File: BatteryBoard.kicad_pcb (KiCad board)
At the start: 4 copper layers, 90.2 x 95.9 mm, 134 parts, among them J1 Keystone-1048, J10 200528-0100, J5 Keystone-1042, J6 Keystone-1042, J7 1824543, J8 Conn_01x06, J9 Keystone-1048, Q1 NX3008NBKS, Q2 MBT2222ADW1T1, Q3 NX3008NBKS, Q4 MBT2222ADW1T1, Q5 NX3008NBKS, Q6 MBT2222ADW1T1, Q7 NX3008NBKS, Q8 MBT2222ADW1T1, U1 S-8209AAA-T8T1U, U10 BTS5090-1EJA, U11 BTS5090-1EJA, U12 PCA9536D, U2 S-8209AAA-T8T1U, U3 MAX17205G+, U4 SIRA99DP-T1-GE3, U5 SIRA99DP-T1-GE3, U6 SIRA99DP-T1-GE3, U7 SIRA99DP-T1-GE3, U8 LTC4412xS6, U9 LTC4412xS6

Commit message: v2.1 (v3?) Partial Updates
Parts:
- removed F10, F12: 10A, Fuse:Fuse_1206_3216Metric
- removed the J7 at (171.0, 99.9)
- removed J8: Conn_01x06, Connector_PinHeader_2.54mm:PinHeader_1x06_P2.54mm_Vertical
- removed U10, U11: BTS5090-1EJA, Package_SO:Infineon_PG-DSO-8-43
- removed U12: PCA9536D, Package_SO:SOIC-8_3.9x4.9mm_P1.27mm
- removed U8, U9: LTC4412xS6, Package_TO_SOT_SMD:TSOT-23-6
- added D8: MMBD452LT1G, Package_TO_SOT_SMD:SOT-23-3, B.Cu at (107.6, 93.9)
- added D9: MMBD452LT1G, Package_TO_SOT_SMD:SOT-23-3, B.Cu at (107.6, 100.7)
- added F5: 10A, Fuse:Fuse_1206_3216Metric, B.Cu at (182.1, 76.7)
- added F8: 6A, Fuse:Fuse_1206_3216Metric, B.Cu at (164.1, 110.2)
- added J5: Fuel Gauge Programming Header, Connector_PinHeader_2.54mm:PinHeader_1x05_P2.54mm_Vertical_SMD_Pin1Left, B.Cu at (160.1, 86.1)
- added Q11: SIRA99DP-T1-GE3, Package_SO:PowerPAK_SO-8_Single, B.Cu at (172.5, 108.9)
- added Q12: SIRA99DP-T1-GE3, Package_SO:PowerPAK_SO-8_Single, B.Cu at (172.5, 101.6)
- added Q13: SIRA99DP-T1-GE3, Package_SO:PowerPAK_SO-8_Single, B.Cu at (160.2, 108.9)
- added Q14: SIRA99DP-T1-GE3, Package_SO:PowerPAK_SO-8_Single, B.Cu at (160.2, 101.7)
- added Q15: NX3008NBKS, Package_TO_SOT_SMD:SOT-363_SC-70-6, B.Cu at (141.4, 80.8)
- added Q16: MBT2222ADW1T1, Package_TO_SOT_SMD:SOT-363_SC-70-6, B.Cu at (145.4, 80.8)
- added Q17: NX3008NBKS, Package_TO_SOT_SMD:SOT-363_SC-70-6, B.Cu at (145.4, 85.6)
- added Q18: MBT2222ADW1T1, Package_TO_SOT_SMD:SOT-363_SC-70-6, B.Cu at (141.4, 85.6)
- added Q19: NX3008NBKS, Package_TO_SOT_SMD:SOT-363_SC-70-6, B.Cu at (125.8, 80.8)
- added Q20: MBT2222ADW1T1, Package_TO_SOT_SMD:SOT-363_SC-70-6, B.Cu at (130.2, 80.8)
- added Q21: NX3008NBKS, Package_TO_SOT_SMD:SOT-363_SC-70-6, B.Cu at (130.2, 85.6)
- added Q22: MBT2222ADW1T1, Package_TO_SOT_SMD:SOT-363_SC-70-6, B.Cu at (125.8, 85.6)
- added Q23: IRLML2803, Package_TO_SOT_SMD:SOT-23, B.Cu at (135.3, 110.6)
- added Q9: Si1442DH, Package_TO_SOT_SMD:SOT-363_SC-70-6, B.Cu at (99.4, 61.2)
- added R62: 10k, Resistor_SMD:R_0603_1608Metric, B.Cu at (141.5, 83.2)
- added R63: 680R, Resistor_SMD:R_0603_1608Metric, B.Cu at (147.4, 80.8)
- added R64: 100k, Resistor_SMD:R_0603_1608Metric, B.Cu at (138.4, 83.2)
- added R65: 200k, Resistor_SMD:R_0603_1608Metric, B.Cu at (138.4, 81.7)
- added R66: 10k, Resistor_SMD:R_0603_1608Metric, B.Cu at (137.8, 85.6)
- added R67: 10k, Resistor_SMD:R_0603_1608Metric, B.Cu at (145.3, 83.2)
- added R68: 680R, Resistor_SMD:R_0603_1608Metric, B.Cu at (139.3, 85.6)
- added R69: 100k, Resistor_SMD:R_0603_1608Metric, B.Cu at (148.3, 83.2)
- added R70: 200k, Resistor_SMD:R_0603_1608Metric, B.Cu at (148.3, 84.7)
- added R71: DNI (0R), Resistor_SMD:R_0603_1608Metric, B.Cu at (143.4, 80.8)
- added R72: DNI (0R), Resistor_SMD:R_0603_1608Metric, B.Cu at (143.4, 85.6)
- added R73: 10k, Resistor_SMD:R_0603_1608Metric, B.Cu at (125.4, 91.4)
- added R74: 10k, Resistor_SMD:R_0603_1608Metric, B.Cu at (125.4, 93.0)
- added R75: 10k, Resistor_SMD:R_0603_1608Metric, B.Cu at (125.4, 94.5)
- added R76: 10k, Resistor_SMD:R_0603_1608Metric, B.Cu at (125.4, 96.0)
- added R77: 10k, Resistor_SMD:R_0603_1608Metric, B.Cu at (125.4, 97.5)
- added R78: 10k, Resistor_SMD:R_0603_1608Metric, B.Cu at (125.4, 99.1)
- added R79: 10k, Resistor_SMD:R_0603_1608Metric, B.Cu at (117.3, 92.9)
- added R80: 10k, Resistor_SMD:R_0603_1608Metric, B.Cu at (133.8, 80.8)
- added R81: 10k, Resistor_SMD:R_0603_1608Metric, B.Cu at (126.0, 83.2)
- added R82: 680R, Resistor_SMD:R_0603_1608Metric, B.Cu at (132.3, 80.8)
- added R83: 100k, Resistor_SMD:R_0603_1608Metric, B.Cu at (122.9, 83.2)
- added R84: 200k, Resistor_SMD:R_0603_1608Metric, B.Cu at (122.9, 81.7)
- added R85: 10k, Resistor_SMD:R_0603_1608Metric, B.Cu at (122.2, 85.6)
- added R86: 10k, Resistor_SMD:R_0603_1608Metric, B.Cu at (130.0, 83.2)
- added R87: 680R, Resistor_SMD:R_0603_1608Metric, B.Cu at (123.7, 85.6)
- added R88: 100k, Resistor_SMD:R_0603_1608Metric, B.Cu at (133.1, 83.2)
- added R89: 200k, Resistor_SMD:R_0603_1608Metric, B.Cu at (133.1, 84.7)
- added R90: DNI (0R), Resistor_SMD:R_0603_1608Metric, B.Cu at (128.0, 80.8)
- added R91: DNI (0R), Resistor_SMD:R_0603_1608Metric, B.Cu at (128.0, 85.6)
- C10: value 0.1uF -> 1nF
- C12, C13: value 10nF -> 0.47uF
- C17, C18: value 10uF -> 10nF; footprint Capacitor_SMD:C_0805_2012Metric -> Capacitor_SMD:C_0603_1608Metric
- C5, C6: value 1nF -> 1uF
- C8: value 0.47uF -> 0.1uF
- C9: value 0.47uF -> 1nF
- D1: value 4.7V -> 10V Vrm; footprint Diode_SMD:D_SMA -> Diode_SMD:D_SOD-123F
- D2: value 10V -> 10V Vrm; footprint Diode_SMD:D_SMA -> Diode_SMD:D_SOD-123F
- D3, D4: value MMBD452LT1G -> GREEN; footprint Package_TO_SOT_SMD:SOT-23-3 -> LED_SMD:LED_0603_1608Metric
- D5: value MMBD452LT1G -> 10V; footprint Package_TO_SOT_SMD:SOT-23-3 -> Diode_SMD:D_SMA
- D6: value 10V Vrm -> 4.7V; footprint Diode_SMD:D_SOD-123F -> Diode_SMD:D_SMA
- D7: value 10V Vrm -> MMBD452LT1G; footprint Diode_SMD:D_SOD-123F -> Package_TO_SOT_SMD:SOT-23-3
- F1: value 1A -> 10A; footprint Fuse:Fuse_0805_2012Metric -> Fuse:Fuse_1206_3216Metric; moved to F.Cu
- F2: value 6A -> 10A; footprint Fuse:Fuse_0805_2012Metric -> Fuse:Fuse_1206_3216Metric; moved to F.Cu
- F3: value 6A -> 10A; footprint Fuse:Fuse_0805_2012Metric -> Fuse:Fuse_1206_3216Metric
- F7: value 10A -> 6A; moved to B.Cu
- F9: value 10A -> 1A; footprint Fuse:Fuse_1206_3216Metric -> Fuse:Fuse_0805_2012Metric; moved to B.Cu
- Q1: value NX3008NBKS -> IRLML2803; footprint Package_TO_SOT_SMD:SOT-363_SC-70-6 -> Package_TO_SOT_SMD:SOT-23
- Q2, Q4: value MBT2222ADW1T1 -> SIRA99DP-T1-GE3; footprint Package_TO_SOT_SMD:SOT-363_SC-70-6 -> Package_SO:PowerPAK_SO-8_Single
- Q3, Q5, Q7: value NX3008NBKS -> Si1442DH; moved to F.Cu
- Q6: value MBT2222ADW1T1 -> Si1442DH; moved to F.Cu
- Q8: value MBT2222ADW1T1 -> Si1442DH
- R10: value 30k -> 100k
- R11: value 30k -> 10k
- R12: value 100K -> 0.05R; footprint Resistor_SMD:R_0603_1608Metric -> Resistor_SMD:R_1206_3216Metric
- R13: value 100K -> 0R
- R14: value 680R -> 10k
- R15: value 100K -> 30k
- R16, R17: value 10K -> 10k
- R18, R39: value 200K -> 10k
- R19: value DNI (0R) -> 2.7k
- R20, R33, R34: value DNI (0R) -> 10R; footprint Resistor_SMD:R_0603_1608Metric -> Resistor_SMD:R_2010_5025Metric; moved to F.Cu
- R21: value 680R -> 10R; footprint Resistor_SMD:R_0603_1608Metric -> Resistor_SMD:R_2010_5025Metric; moved to F.Cu
- R22, R36: value 100K -> 10R; footprint Resistor_SMD:R_0603_1608Metric -> Resistor_SMD:R_2010_5025Metric; moved to F.Cu
- R23, R31: value 10K -> 10k; moved to F.Cu
- R24, R37, R38: value 10K -> 10R; footprint Resistor_SMD:R_0603_1608Metric -> Resistor_SMD:R_2010_5025Metric; moved to F.Cu
- R25, R32: value 200K -> 10R; footprint Resistor_SMD:R_0603_1608Metric -> Resistor_SMD:R_2010_5025Metric; moved to F.Cu
- R26: value 1k -> 10R; footprint Resistor_SMD:R_0603_1608Metric -> Resistor_SMD:R_2010_5025Metric; moved to F.Cu
- R27: value 1k -> 10k
- R28: value 680R -> 10R; footprint Resistor_SMD:R_0603_1608Metric -> Resistor_SMD:R_2010_5025Metric
- R29: value 100K -> 10R; footprint Resistor_SMD:R_0603_1608Metric -> Resistor_SMD:R_2010_5025Metric
- R3: value 10R -> 470R
- R30: value 10K -> 10R; footprint Resistor_SMD:R_0603_1608Metric -> Resistor_SMD:R_2010_5025Metric
- R35: value 680R -> 10k; moved to F.Cu
- R4, R5: value 470R -> 1k
- R40, R41: value 160R -> 10R; moved to B.Cu
- R42: value 160R -> 10R
- R43: value 160R -> 10k; footprint Resistor_SMD:R_2010_5025Metric -> Resistor_SMD:R_0603_1608Metric; moved to F.Cu
- R44: value 160R -> 470k; footprint Resistor_SMD:R_2010_5025Metric -> Resistor_SMD:R_0603_1608Metric; moved to B.Cu
- R45: value 160R -> 100k; footprint Resistor_SMD:R_2010_5025Metric -> Resistor_SMD:R_0603_1608Metric; moved to B.Cu
- R47: value 100k -> 470k; footprint Capacitor_SMD:C_0603_1608Metric -> Resistor_SMD:R_0603_1608Metric
- R48: value 100k -> 10R
- R49: value 100k -> 100R; footprint Capacitor_SMD:C_0603_1608Metric -> Resistor_SMD:R_0603_1608Metric
- R50: value 160R -> 10m; footprint Resistor_SMD:R_2010_5025Metric -> Resistor_SMD:R_2512_6332Metric; moved to B.Cu
- R51: value 160R -> 1k; footprint Resistor_SMD:R_2010_5025Metric -> Resistor_SMD:R_0603_1608Metric; moved to B.Cu
- R52, R53: value 160R -> 30k; footprint Resistor_SMD:R_2010_5025Metric -> Resistor_SMD:R_0603_1608Metric
- R54: value 160R -> 51.1k; footprint Resistor_SMD:R_2010_5025Metric -> Resistor_SMD:R_0603_1608Metric; moved to B.Cu
- R55, R56, R57: value 160R -> 150R; footprint Resistor_SMD:R_2010_5025Metric -> Resistor_SMD:R_0603_1608Metric; moved to B.Cu
- R58: value 160R -> 10k; footprint Resistor_SMD:R_2010_5025Metric -> Resistor_SMD:R_0603_1608Metric
- R59: value 160R -> 0R; footprint Resistor_SMD:R_2010_5025Metric -> Resistor_SMD:R_0603_1608Metric
- R6: value 1k -> 470R
- R60: value 160R -> 0R; footprint Resistor_SMD:R_2010_5025Metric -> Resistor_SMD:R_0603_1608Metric; moved to B.Cu
- R61: value 160R -> 10k; footprint Resistor_SMD:R_2010_5025Metric -> Resistor_SMD:R_0603_1608Metric; moved to B.Cu
- R7: value 1k -> 2.7k
- R8: value 100R -> 10k
- R9: value 10m -> 10k; footprint Resistor_SMD:R_2512_6332Metric -> Resistor_SMD:R_0603_1608Metric
- TH4: moved to B.Cu
- TH6: moved to F.Cu
- U3: value MAX17205G+ -> MAX4211B/E; footprint Argus-IC:21-0137_T1433&plus_2C_MXM -> Package_DFN_QFN:QFN-16-1EP_4x4mm_P0.65mm_EP2.1x2.1mm
- U4, U5: value SIRA99DP-T1-GE3 -> LTC4412xS6; footprint Argus-Misc:MOSFET_7DP-T1-GE3_VIS -> Package_TO_SOT_SMD:TSOT-23-6
- U6: value SIRA99DP-T1-GE3 -> MAX17205; footprint Argus-Misc:MOSFET_7DP-T1-GE3_VIS -> Package_DFN_QFN:TDFN-14-1EP_3x3mm_P0.4mm_EP1.78x2.35mm
- U7: value SIRA99DP-T1-GE3 -> MAX7310; footprint Argus-Misc:MOSFET_7DP-T1-GE3_VIS -> Package_DFN_QFN:QFN-16-1EP_4x4mm_P0.65mm_EP2.1x2.1mm
- moved TH5 81.2 mm to (116.1, 67.1)
- moved D6 80.7 mm to (107.3, 88.6), turned to 90 degrees
- moved TH1 77.2 mm to (164.6, 126.5), turned to -90 degrees
- moved TH2 77.2 mm to (164.6, 126.5), turned to 90 degrees
- moved D7 75.7 mm to (107.6, 97.3), turned to 180 degrees
- moved F1 68.7 mm to (182.1, 76.7)
- moved TH4 67.7 mm to (116.1, 67.1), turned to 90 degrees
- moved TH6 67.6 mm to (116.1, 86.3), turned to -90 degrees
- moved F3 63.6 mm to (182.4, 60.7)
- moved D5 63.5 mm to (177.0, 96.8), turned to 90 degrees
- moved F9 63.5 mm to (119.5, 90.2), turned to 180 degrees
- moved D1 62.5 mm to (175.5, 79.8), turned to 0 degrees
- moved REF** 62.3 mm to (209.5, 59.2)
- moved Q3 62.1 mm to (99.4, 120.6), turned to 180 degrees
- moved R45 62.0 mm to (176.1, 105.3), turned to -90 degrees
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- renumbered J9 to J2, J6 to J3, J5 to J4, J10 to J7
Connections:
- C1 pad 2: /Battery/BATT1 -> /Battery Bus Detection/BATT_N
- C10 pad 1: SYSTEM_VDD -> Net-(U6-CELL1)
- C10 pad 2: GND -> /Battery Bus Detection/BATT_N
- C11 pad 1: Net-(U9-VIN) -> Net-(U6-VBATT)
- C11 pad 2: GND -> SYSTEM_VSS
- C12 pad 1: Net-(Q1B-G) -> Net-(U6-REG2)
- C12 pad 2: GND -> SYSTEM_VSS
- C13 pad 1: Net-(Q3B-G) -> Net-(U6-REG3)
- C13 pad 2: GND -> SYSTEM_VSS
- C14 pad 1: Net-(Q5B-G) -> Net-(Q15B-G)
- C15 pad 1: Net-(Q7B-G) -> Net-(Q17B-G)
- C16 pad 1: +3V3 -> Net-(U7-V+)
- C17 pad 1: /Interfaces/+3V3_PS -> Net-(Q19B-G)
- C18 pad 1: SYSTEM_VDD -> Net-(Q21B-G)
- C19 pad 1: SYSTEM_VDD -> +3V3
- C2 pad 2: /Battery/BATT1 -> /Battery Bus Detection/BATT_N
- C3 pad 2: /Battery Monitor/CSP -> /Battery Bus Detection/BATT_M
- C4 pad 2: /Battery Monitor/CSP -> /Battery Bus Detection/BATT_M
- C5 pad 1: /Battery Monitor/CELL1 -> /Battery Temperature Protection/ON/~{OFF}
- C5 pad 2: /Battery Monitor/CSP -> GND
- C6 pad 1: /Battery Monitor/CELL2 -> Net-(C6-Pad1)
- C6 pad 2: /Battery Monitor/CELL1 -> VBUS
- C7 pad 1: /Battery Monitor/CELL2 -> SYSTEM_VDD
- C8 pad 1: /Battery Monitor/REG3 -> Net-(Q13-D)
- C9 pad 1: /Battery Monitor/REG2 -> Net-(U6-VBATT)
- C9 pad 2: SYSTEM_VSS -> Net-(U6-CELL1)
- D1 pad 1: +3V3 -> /Battery Bus Detection/BATT_M
- D1 pad 2: GND -> /Battery Bus Detection/BATT_N
- D2 pad 1: SYSTEM_VDD -> /Battery Bus Detection/BATT_P
- D2 pad 2: SYSTEM_VSS -> /Battery Bus Detection/BATT_M
- D3 pad 2: /Battery Monitor/ALERT -> Net-(D3-A)
- D4 pad 2: /Interfaces/SCL_BUS -> Net-(D4-A)
- D5 pad 1: GND -> SYSTEM_VDD
- D5 pad 2: /Interfaces/SDA_BUS -> SYSTEM_VSS
- D6 pad 1: /Battery/BATT2 -> +3V3
- D6 pad 2: /Battery/BATT1 -> GND
- D7 pad 1: /Battery/BATT1 -> GND
- D7 pad 2: /Battery Monitor/CSP -> +3V3
- F1 pad 1: /Interfaces/+3V3_PS -> Net-(F1-Pad1)
- F1 pad 2: +3V3 -> Net-(F1-Pad2)
- F2 pad 1: /Battery/BATT2 -> Net-(F2-Pad1)
- F3 pad 1: Net-(F3-Pad1) -> Net-(F1-Pad2)
- F3 pad 2: /Battery/BATT2 -> Net-(J3-NEG)
- F4 pad 1: Net-(J5-POS) -> Net-(F2-Pad2)
- F4 pad 2: /Battery/BATT2 -> Net-(J4-POS)
- F6 pad 1: Net-(J6-NEG) -> Net-(J4-POS)
- F6 pad 2: /Battery Monitor/CSP -> /Battery Bus Detection/BATT_P
- F7 pad 1: Net-(F10-Pad2) -> /Battery Bus Detection/BATT_P
- F7 pad 2: Net-(J5-POS) -> Net-(Q11-D)
- F9 pad 1: Net-(F12-Pad2) -> Net-(U7-V+)
- F9 pad 2: Net-(J6-NEG) -> +3V3
- J1 pad 1: Net-(F12-Pad1) -> Net-(F1-Pad1)
- J1 pad 2: /Battery/BATT1 -> /Battery Bus Detection/BATT_M
- J1 pad 3: Net-(F12-Pad2) -> Net-(F1-Pad2)
- J1 pad 4: /Battery/BATT1 -> /Battery Bus Detection/BATT_M
- J2 pad 1: /Battery/BATT1 -> /Battery Bus Detection/BATT_M
- J2 pad 2: Net-(F10-Pad1) -> Net-(F2-Pad1)
- J2 pad 3: /Battery/BATT1 -> /Battery Bus Detection/BATT_M
- J2 pad 4: Net-(F10-Pad2) -> Net-(F2-Pad2)
- J3 pad 1: Net-(J6-NEG) -> Net-(J3-NEG)
- J3 pad 2: /Battery/BATT1 -> /Battery Bus Detection/BATT_M
- J4 pad 1: /Battery/BATT1 -> /Battery Bus Detection/BATT_M
- J4 pad 2: Net-(J5-POS) -> Net-(J4-POS)
- J7 pad 10: /Interfaces/+3V3_PS -> +3V3
- J7 pad 4: /Battery Monitor/ALERT -> /Interfaces/ALERT
- J7 pad 9: /Interfaces/+3V3_PS -> +3V3
- Q1 pad 1: GND -> Net-(Q1-G)
- Q1 pad 2: Net-(Q1A-G) -> GND
- Q1 pad 3: Net-(Q1A-G) -> /Battery Temperature Protection/~{FAULT}
- Q2 pad 1: /Interfaces/SCL_BUS -> Net-(U3-RS-)
- Q2 pad 2: Net-(Q2A-B1) -> Net-(U3-RS-)
- Q2 pad 3: /Interfaces/SCL_BUS -> Net-(U3-RS-)
- Q2 pad 4: /Battery Monitor/SCL -> Net-(Q1-G)
- Q2 pad 5: Net-(Q1A-D) -> VBUS
- Q3 pad 1: GND -> Net-(Q3-D-Pad1)
- Q3 pad 2: Net-(Q3A-G) -> Net-(Q3-D-Pad1)
- Q3 pad 3: Net-(Q3A-G) -> /Battery Temperature Protection/HEATER_ENABLE1
- Q3 pad 4: GND -> SYSTEM_VSS
- Q3 pad 5: Net-(Q3B-G) -> Net-(Q3-D-Pad1)
- Q3 pad 6: Net-(Q3A-D) -> Net-(Q3-D-Pad1)
- Q4 pad 1: /Interfaces/SDA_BUS -> SYSTEM_VDD
- Q4 pad 2: Net-(Q4A-B1) -> SYSTEM_VDD
- Q4 pad 3: /Interfaces/SDA_BUS -> SYSTEM_VDD
- Q4 pad 4: /Battery Monitor/SDA -> Net-(Q23-D)
- Q4 pad 5: Net-(Q3A-D) -> Net-(Q4-D)
- Q5 pad 1: GND -> Net-(Q5-D-Pad1)
- Q5 pad 2: Net-(Q5A-G) -> Net-(Q5-D-Pad1)
- Q5 pad 3: Net-(Q5A-G) -> /Battery Temperature Protection/HEATER_ENABLE0
- Q5 pad 4: GND -> SYSTEM_VSS
- Q5 pad 5: Net-(Q5B-G) -> Net-(Q5-D-Pad1)
- Q5 pad 6: Net-(Q5A-D) -> Net-(Q5-D-Pad1)
- Q6 pad 1: /Interfaces/SCL_BUS -> Net-(Q6-D-Pad1)
- Q6 pad 2: Net-(Q6A-B1) -> Net-(Q6-D-Pad1)
- Q6 pad 3: /Interfaces/SCL_BUS -> /Battery Temperature Protection/HEATER_ENABLE1
- Q6 pad 4: /IO Expander/SCL -> SYSTEM_VSS
- Q6 pad 5: Net-(Q5A-D) -> Net-(Q6-D-Pad1)
- Q6 pad 6: /IO Expander/SCL -> Net-(Q6-D-Pad1)
- Q7 pad 1: GND -> Net-(Q7-D-Pad1)
- Q7 pad 2: Net-(Q7A-G) -> Net-(Q7-D-Pad1)
- Q7 pad 3: Net-(Q7A-G) -> /Battery Temperature Protection/HEATER_ENABLE0
- Q7 pad 4: GND -> SYSTEM_VSS
- Q7 pad 5: Net-(Q7B-G) -> Net-(Q7-D-Pad1)
- Q7 pad 6: Net-(Q7A-D) -> Net-(Q7-D-Pad1)
- Q8 pad 1: /Interfaces/SDA_BUS -> Net-(Q8-D-Pad1)
- Q8 pad 2: Net-(Q8A-B1) -> Net-(Q8-D-Pad1)
- Q8 pad 3: /Interfaces/SDA_BUS -> /Battery Temperature Protection/HEATER_ENABLE1
- Q8 pad 4: /IO Expander/SDA -> SYSTEM_VSS
- Q8 pad 5: Net-(Q7A-D) -> Net-(Q8-D-Pad1)
- Q8 pad 6: /IO Expander/SDA -> Net-(Q8-D-Pad1)
- R1 pad 2: Net-(U2-CO) -> /Battery Bus Detection/BATT_N
- R10 pad 1: VTHERM -> GND
- R10 pad 2: /Battery Monitor/THERM2 -> Net-(C6-Pad1)
- R11 pad 1: VTHERM -> Net-(U3-INHIBIT)
- R11 pad 2: /Battery Monitor/THERM1 -> Net-(C6-Pad1)
- R12 pad 1: Net-(U8-SENSE) -> Net-(Q4-D)
- R12 pad 2: /Battery Bus Detection/CHARGE_EN -> Net-(U3-RS-)
- R13 pad 1: Net-(F3-Pad1) -> Net-(U3-CIN1+)
- R13 pad 2: /Battery Bus Detection/DISCHARGE_EN -> Net-(U3-IOUT)
- R14 pad 1: Net-(Q2A-B1) -> Net-(U3-CIN1-)
- R14 pad 2: Net-(Q1A-D) -> Net-(U3-CIN2+)
- R15 pad 1: +3V3 -> GND
- R15 pad 2: Net-(Q1A-G) -> Net-(U3-CIN1-)
- R16 pad 1: +3V3 -> GND
- R16 pad 2: Net-(Q1A-D) -> /Battery Temperature Protection/CB-RESET
- R17 pad 1: +3V3 -> Net-(Q1-G)
- R17 pad 2: /Battery Monitor/SCL -> Net-(U3-RS-)
- R18 pad 1: /Battery Monitor/SCL -> /Battery Temperature Protection/~{FAULT}
- R18 pad 2: Net-(Q1B-G) -> +3V3
- R19 pad 1: /Battery Monitor/SCL -> Net-(D4-A)
- R19 pad 2: /Interfaces/SCL_BUS -> VBUS
- R2 pad 2: Net-(U2-DO) -> /Battery Bus Detection/BATT_N
- R20 pad 1: /Battery Monitor/SDA -> Net-(R20-Pad1)
- R20 pad 2: /Interfaces/SDA_BUS -> VBUS
- R21 pad 1: Net-(Q4A-B1) -> Net-(R21-Pad1)
- R21 pad 2: Net-(Q3A-D) -> Net-(R20-Pad1)
- R22 pad 1: +3V3 -> Net-(Q5-D-Pad1)
- R22 pad 2: Net-(Q3A-G) -> Net-(R21-Pad1)
- R23 pad 1: +3V3 -> SYSTEM_VSS
- R23 pad 2: Net-(Q3A-D) -> /Battery Temperature Protection/HEATER_ENABLE0
- R24 pad 1: +3V3 -> Net-(R24-Pad1)
- R24 pad 2: /Battery Monitor/SDA -> VBUS
- R25 pad 1: /Battery Monitor/SDA -> Net-(R25-Pad1)
- R25 pad 2: Net-(Q3B-G) -> Net-(R24-Pad1)
- R26 pad 1: Net-(U10-DEN) -> Net-(Q7-D-Pad1)
- R26 pad 2: GND -> Net-(R25-Pad1)
- R27 pad 1: Net-(U11-DEN) -> SYSTEM_VSS
- R27 pad 2: GND -> /Battery Temperature Protection/HEATER_ENABLE0
- R28 pad 1: Net-(Q6A-B1) -> Net-(R28-Pad1)
- R28 pad 2: Net-(Q5A-D) -> VBUS
- R29 pad 1: +3V3 -> Net-(R29-Pad1)
- R29 pad 2: Net-(Q5A-G) -> Net-(R28-Pad1)
- R3 pad 1: /Battery/BATT2 -> /Battery Bus Detection/BATT_M
- R3 pad 2: /Battery Monitor/CELL2 -> Net-(U1-VDD)
- R30 pad 1: +3V3 -> Net-(Q9-D-Pad1)
- R30 pad 2: Net-(Q5A-D) -> Net-(R29-Pad1)
- R31 pad 1: +3V3 -> SYSTEM_VSS
- R31 pad 2: /IO Expander/SCL -> /Battery Temperature Protection/HEATER_ENABLE0
- R32 pad 1: /IO Expander/SCL -> Net-(R32-Pad1)
- R32 pad 2: Net-(Q5B-G) -> VBUS
- R33 pad 1: /IO Expander/SCL -> Net-(R33-Pad1)
- R33 pad 2: /Interfaces/SCL_BUS -> Net-(R32-Pad1)
- R34 pad 1: /IO Expander/SDA -> Net-(Q3-D-Pad1)
- R34 pad 2: /Interfaces/SDA_BUS -> Net-(R33-Pad1)
- R35 pad 1: Net-(Q8A-B1) -> SYSTEM_VSS
- R35 pad 2: Net-(Q7A-D) -> /Battery Temperature Protection/HEATER_ENABLE1
- R36 pad 1: +3V3 -> Net-(R36-Pad1)
- R36 pad 2: Net-(Q7A-G) -> VBUS
- R37 pad 1: +3V3 -> Net-(R37-Pad1)
- R37 pad 2: Net-(Q7A-D) -> Net-(R36-Pad1)
- R38 pad 1: +3V3 -> Net-(Q6-D-Pad1)
- R38 pad 2: /IO Expander/SDA -> Net-(R37-Pad1)
- R39 pad 1: /IO Expander/SDA -> SYSTEM_VSS
- R39 pad 2: Net-(Q7B-G) -> /Battery Temperature Protection/HEATER_ENABLE1
- R4 pad 1: /Battery/BATT2 -> Net-(U2-CTLC)
- R4 pad 2: Net-(U1-VDD) -> Net-(U1-CO)
- R40 pad 1: /Battery Temperature Protection/HEATER -> Net-(R40-Pad1)
- R40 pad 2: Net-(R40-Pad2) -> VBUS
- R41 pad 1: /Battery Temperature Protection/HEATER -> Net-(R41-Pad1)
- R41 pad 2: Net-(R41-Pad2) -> Net-(R40-Pad1)
- R42 pad 1: /Battery Temperature Protection/HEATER -> Net-(Q8-D-Pad1)
- R42 pad 2: Net-(R42-Pad2) -> Net-(R41-Pad1)
- R43 pad 1: /Battery Temperature Protection1/HEATER -> SYSTEM_VSS
- R43 pad 2: Net-(R43-Pad2) -> /Battery Temperature Protection/HEATER_ENABLE1
- R44 pad 1: /Battery Temperature Protection1/HEATER -> +3V3
- R44 pad 2: Net-(R44-Pad2) -> /Battery Bus Protection/CHARGE_ACTIVE
- R45 pad 1: /Battery Temperature Protection1/HEATER -> Net-(U4-SENSE)
- R45 pad 2: Net-(R45-Pad2) -> /Battery Bus Detection/CHARGE_EN
- R46 pad 1: GND -> Net-(F8-Pad1)
- R46 pad 2: /IO Expander/IO0 -> /Battery Bus Detection/DISCHARGE_EN
- R47 pad 1: GND -> +3V3
- R47 pad 2: /IO Expander/IO2 -> /Battery Bus Protection/DISCHARGE_ACTIVE
- R48 pad 1: GND -> /Battery Bus Detection/BATT_P
- R48 pad 2: /IO Expander/IO1 -> Net-(U6-VBATT)
- R49 pad 1: GND -> /Battery Bus Detection/BATT_M
- R49 pad 2: /IO Expander/IO3 -> Net-(U6-CELL1)
- R5 pad 1: /Battery/BATT1 -> Net-(U2-CTLD)
- R5 pad 2: Net-(U2-VDD) -> Net-(U1-DO)
- R50 pad 1: Net-(R40-Pad2) -> SYSTEM_VSS
- R50 pad 2: Net-(R50-Pad2) -> /Battery Bus Detection/BATT_N
- R51 pad 1: Net-(R41-Pad2) -> Net-(U6-ALRT1)
- R51 pad 2: Net-(R51-Pad2) -> /Interfaces/ALERT
- R52 pad 1: Net-(R42-Pad2) -> Net-(U6-THRM)
- R52 pad 2: Net-(R52-Pad2) -> Net-(U6-AIN2)
- R53 pad 1: Net-(R43-Pad2) -> Net-(U6-THRM)
- R53 pad 2: Net-(R53-Pad2) -> Net-(U6-AIN1)
- R54 pad 1: Net-(R44-Pad2) -> /Interfaces/ALERT
- R54 pad 2: Net-(R54-Pad2) -> /Battery Monitor/A
- R55 pad 1: Net-(R45-Pad2) -> /Battery Monitor/SDA
- R55 pad 2: Net-(R55-Pad2) -> /Battery Monitor/DQ
- R56 pad 1: Net-(R50-Pad2) -> /Battery Monitor/SDA
- R56 pad 2: SYSTEM_VSS -> /Battery Monitor/D
- R57 pad 1: Net-(R51-Pad2) -> /Battery Monitor/SCL
- R57 pad 2: SYSTEM_VSS -> /Battery Monitor/C
- R58 pad 1: Net-(R52-Pad2) -> /Interfaces/ALERT
- R58 pad 2: SYSTEM_VSS -> +3V3
- R59 pad 1: Net-(R53-Pad2) -> /Battery Monitor/SCL
- R59 pad 2: SYSTEM_VSS -> /Battery Monitor/I2C Protection/SCL_DEVICE
- R6 pad 1: Net-(U2-CTLD) -> /Battery Bus Detection/BATT_P
- R6 pad 2: /Battery Monitor/CSP -> Net-(U2-VDD)
- R60 pad 1: Net-(R54-Pad2) -> /Battery Monitor/I2C Protection/SDA_DEVICE
- R60 pad 2: SYSTEM_VSS -> /Battery Monitor/SDA
- R61 pad 1: Net-(R55-Pad2) -> +3V3
- R61 pad 2: SYSTEM_VSS -> Net-(Q15A-D)
- R7 pad 1: Net-(U2-CTLC) -> /Battery Temperature Protection/ON/~{OFF}
- R7 pad 2: /Battery Monitor/CSP -> Net-(D3-A)
- R8 pad 1: /Battery/BATT1 -> GND
- R8 pad 2: /Battery Monitor/CELL1 -> /Battery Temperature Protection/ON/~{OFF}
- R9 pad 1: SYSTEM_VSS -> Net-(Q23-D)
- R9 pad 2: /Battery Monitor/CSP -> SYSTEM_VDD
- TH1 pad 1: /Battery Monitor/THERM2 -> Net-(U6-AIN2)
- TH4 pad 1: /Battery Monitor/THERM1 -> Net-(U6-AIN1)
- U1 pad 5: /Battery/BATT1 -> /Battery Bus Detection/BATT_N
- U1 pad 6: /Battery Bus Detection/DISCHARGE_EN -> Net-(U1-DO)
- U1 pad 7: /Battery Bus Detection/CHARGE_EN -> Net-(U1-CO)
- U2 pad 5: /Battery Monitor/CSP -> /Battery Bus Detection/BATT_M
- U2 pad 6: Net-(U2-DO) -> /Battery Bus Detection/DISCHARGE_EN
- U2 pad 7: Net-(U2-CO) -> /Battery Bus Detection/CHARGE_EN
- U3 pad 1: /Battery Monitor/REG3 -> /Battery Temperature Protection/ON/~{OFF}
- U3 pad 10: /Battery Monitor/THERM2 -> Net-(U3-CIN1+)
- U3 pad 11: /Battery Monitor/SCL -> Net-(U3-CIN1-)
- U3 pad 12: /Battery Monitor/SDA -> Net-(U3-CIN2+)
- U3 pad 14: VTHERM -> Net-(U3-IOUT)
- U3 pad 15: SYSTEM_VSS -> Net-(U3-RS-)
- U3 pad 2: /Battery Monitor/CSP -> (no net)
- U3 pad 3: /Battery Monitor/REG2 -> Net-(Q1-G)
- U3 pad 4: SYSTEM_VSS -> Net-(Q1-G)
- U3 pad 5: /Battery Monitor/CELL2 -> Net-(U3-INHIBIT)
- U3 pad 6: /Battery Monitor/CELL1 -> Net-(Q1-G)
- U3 pad 7: /Battery Monitor/CELL1 -> GND
- U3 pad 8: /Battery Monitor/ALERT -> Net-(U3-CIN2+)
- U3 pad 9: /Battery Monitor/THERM1 -> /Battery Temperature Protection/CB-RESET
- U4 pad 1: Net-(F3-Pad1) -> SYSTEM_VDD
- U4 pad 2: Net-(F3-Pad1) -> SYSTEM_VSS
- U4 pad 3: Net-(F3-Pad1) -> SYSTEM_VSS
- U4 pad 4: /Battery Bus Detection/DISCHARGE_EN -> /Battery Bus Protection/CHARGE_ACTIVE
- U4 pad 5: Net-(U9-VIN) -> Net-(Q12-G)
- U4 pad 6: Net-(U9-VIN) -> Net-(U4-SENSE)
- U5 pad 1: SYSTEM_VDD -> Net-(Q13-D)
- U5 pad 2: SYSTEM_VDD -> SYSTEM_VSS
- U5 pad 3: SYSTEM_VDD -> SYSTEM_VSS
- U5 pad 4: Net-(U5-G) -> /Battery Bus Protection/DISCHARGE_ACTIVE
- U5 pad 5: Net-(U9-VIN) -> Net-(Q14-G)
- U5 pad 6: Net-(U9-VIN) -> SYSTEM_VDD
- U6 pad 1: Net-(U8-SENSE) -> Net-(U6-REG3)
- U6 pad 2: Net-(U8-SENSE) -> /Battery Bus Detection/BATT_N
- U6 pad 3: Net-(U8-SENSE) -> Net-(U6-REG2)
- U6 pad 4: /Battery Bus Detection/CHARGE_EN -> SYSTEM_VSS
- U6 pad 5: Net-(F2-Pad2) -> Net-(U6-VBATT)
- U6 pad 6: Net-(F2-Pad2) -> Net-(U6-CELL1)
- U6 pad 7: Net-(F2-Pad2) -> Net-(U6-CELL1)
- U6 pad 8: Net-(F2-Pad2) -> Net-(U6-ALRT1)
- U7 pad 1: Net-(U8-SENSE) -> /IO Expander/AD0
- U7 pad 2: Net-(U8-SENSE) -> /IO Expander/AD1
- U7 pad 3: Net-(U8-SENSE) -> /IO Expander/AD2
- U7 pad 4: Net-(U7-G) -> /Battery Temperature Protection/ON/~{OFF}
- U7 pad 5: SYSTEM_VDD -> /Battery Temperature Protection/~{FAULT}
- U7 pad 6: SYSTEM_VDD -> GND
- U7 pad 7: SYSTEM_VDD -> /Battery Temperature Protection/CB-RESET
- U7 pad 8: SYSTEM_VDD -> /Battery Temperature Protection/HEATER_ENABLE0
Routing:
- net /Battery/BATT1: track 270.4 -> 0.00 mm, vias 8 -> 0
- net +3V3: track 172.2 -> 15.4 mm, vias 0 -> 3
- net SYSTEM_VSS: track 182.9 -> 26.4 mm, vias 6 -> 33
- net /Battery Bus Protection/CHARGE_ACTIVE: track 0.00 -> 88.9 mm, vias 0 -> 2
- net Net-(U6-AIN1): track 0.00 -> 85.5 mm, vias 0 -> 2
- net /Battery Temperature Protection/HEATER_ENABLE0: track 0.00 -> 84.2 mm, vias 0 -> 4
- net /Interfaces/ALERT: track 0.00 -> 82.0 mm, vias 0 -> 2
- net /Battery Monitor/ALERT: track 81.3 -> 0.00 mm, vias 2 -> 0
- net /Battery Bus Protection/DISCHARGE_ACTIVE: track 0.00 -> 80.0 mm, vias 0 -> 2
- net /Battery Temperature Protection/HEATER_ENABLE1: track 0.00 -> 73.6 mm, vias 0 -> 4
- net /Battery Monitor/THERM2: track 73.1 -> 0.00 mm
- net /Battery/BATT2: track 71.6 -> 0.00 mm, vias 2 -> 0
- net /Battery Monitor/CSP: track 71.0 -> 0.00 mm, vias 3 -> 0
- net Net-(U6-AIN2): track 0.00 -> 70.8 mm, vias 0 -> 2
- net SYSTEM_VDD: track 45.2 -> 0.00 mm
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- added copper zone on B.Cu, net +3V3
- added copper zone on F.Cu, net /Battery Bus Detection/BATT_M
- added copper zone on B.Cu, net /Battery Bus Detection/BATT_N
- added copper zone on In1.Cu, net /Battery Bus Detection/BATT_N
- added copper zone on B.Cu, net /Battery Bus Detection/BATT_P
- added copper zone on In2.Cu, net /Battery Bus Detection/BATT_P
- added copper zone on B.Cu, net /Battery Bus Detection/CHARGE_EN
- added copper zone on B.Cu, net /Battery Bus Detection/DISCHARGE_EN
- added copper zone on F.Cu, net Net-(F1-Pad1)
- added copper zone on B.Cu, net Net-(F1-Pad2)
- added copper zone on F.Cu, net Net-(F1-Pad2)
- added copper zone on F.Cu, net Net-(F2-Pad1)
- added copper zone on F.Cu, net Net-(F2-Pad2)
- added copper zone on B.Cu, net Net-(F8-Pad1)
- added copper zone on B.Cu, net Net-(J3-NEG)
- added copper zone on B.Cu, net Net-(J4-POS)
- added copper zone on B.Cu, net Net-(Q11-D)
- added copper zone on B.Cu, net Net-(Q12-G)
- added copper zone on B.Cu, net Net-(Q13-D)
- added copper zone on B.Cu, net Net-(Q14-G)
- added copper zone on F.Cu, net Net-(Q3-D-Pad1)
- added copper zone on In2.Cu, net Net-(Q3-D-Pad1)
- added copper zone on B.Cu, net Net-(Q4-D)
- added copper zone on F.Cu, net Net-(Q5-D-Pad1)
- added copper zone on In2.Cu, net Net-(Q5-D-Pad1)
- added copper zone on F.Cu, net Net-(Q6-D-Pad1)
- added copper zone on In2.Cu, net Net-(Q6-D-Pad1)
- added copper zone on F.Cu, net Net-(Q7-D-Pad1)
- added copper zone on In2.Cu, net Net-(Q7-D-Pad1)
- added copper zone on B.Cu, net Net-(Q8-D-Pad1)
- added copper zone on B.Cu, net Net-(Q9-D-Pad1)
- added copper zone on B.Cu, net Net-(U3-RS-)
- added copper zone on B.Cu, net Net-(U4-SENSE)
- added copper zone on B.Cu, net Net-(U7-V+)
- added copper zone on F.Cu, net SYSTEM_VSS
- added copper zone on In1.Cu, net SYSTEM_VSS
- added copper zone on B.Cu, net VBUS
- added copper zone on F.Cu, net VBUS
- added copper zone on In2.Cu, net VBUS
- removed copper zone on B.Cu, net /Battery Monitor/CSP
- removed copper zone on B.Cu, net /Battery Temperature Protection/HEATER
- removed copper zone on B.Cu, net /Battery Temperature Protection1/HEATER
- removed copper zone on B.Cu, net /Battery/BATT1
- removed copper zone on F.Cu, net /Battery/BATT1
- removed copper zone on B.Cu, net /Battery/BATT2
- removed copper zone on B.Cu, net /Interfaces/+3V3_PS
- removed copper zone on F.Cu, net GND
- removed copper zone on F.Cu, net Net-(F10-Pad1)
- removed copper zone on F.Cu, net Net-(F10-Pad2)
- removed copper zone on F.Cu, net Net-(F12-Pad1)
- removed copper zone on F.Cu, net Net-(F12-Pad2)
- removed copper zone on B.Cu, net Net-(F3-Pad1)
- removed copper zone on B.Cu, net Net-(J5-POS)
- removed copper zone on F.Cu, net Net-(J5-POS)
- removed copper zone on B.Cu, net Net-(J6-NEG)
- removed copper zone on F.Cu, net Net-(J6-NEG)
- removed copper zone on B.Cu, net Net-(U8-SENSE)
- removed copper zone on B.Cu, net Net-(U9-VIN)
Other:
- outline, holes or cut-outs redrawn

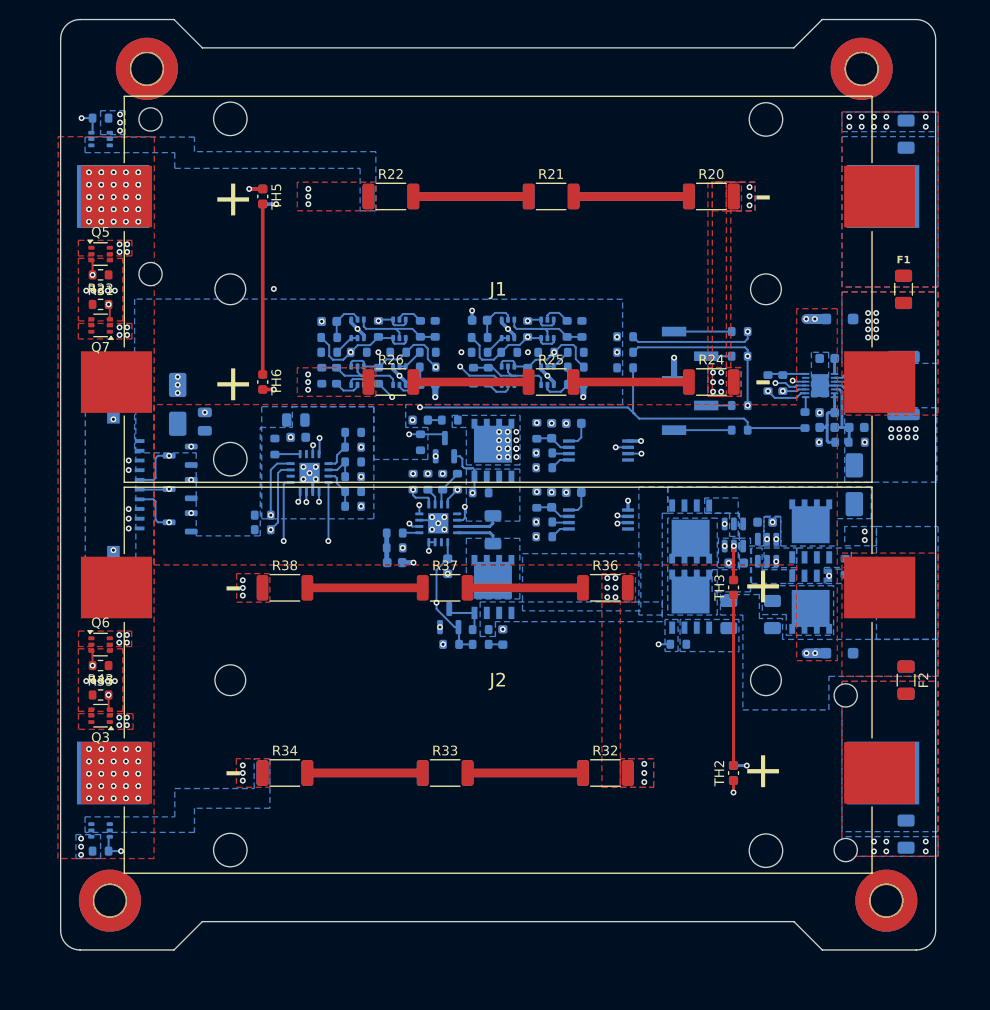
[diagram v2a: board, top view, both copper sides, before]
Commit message: Silkscreen cleanup
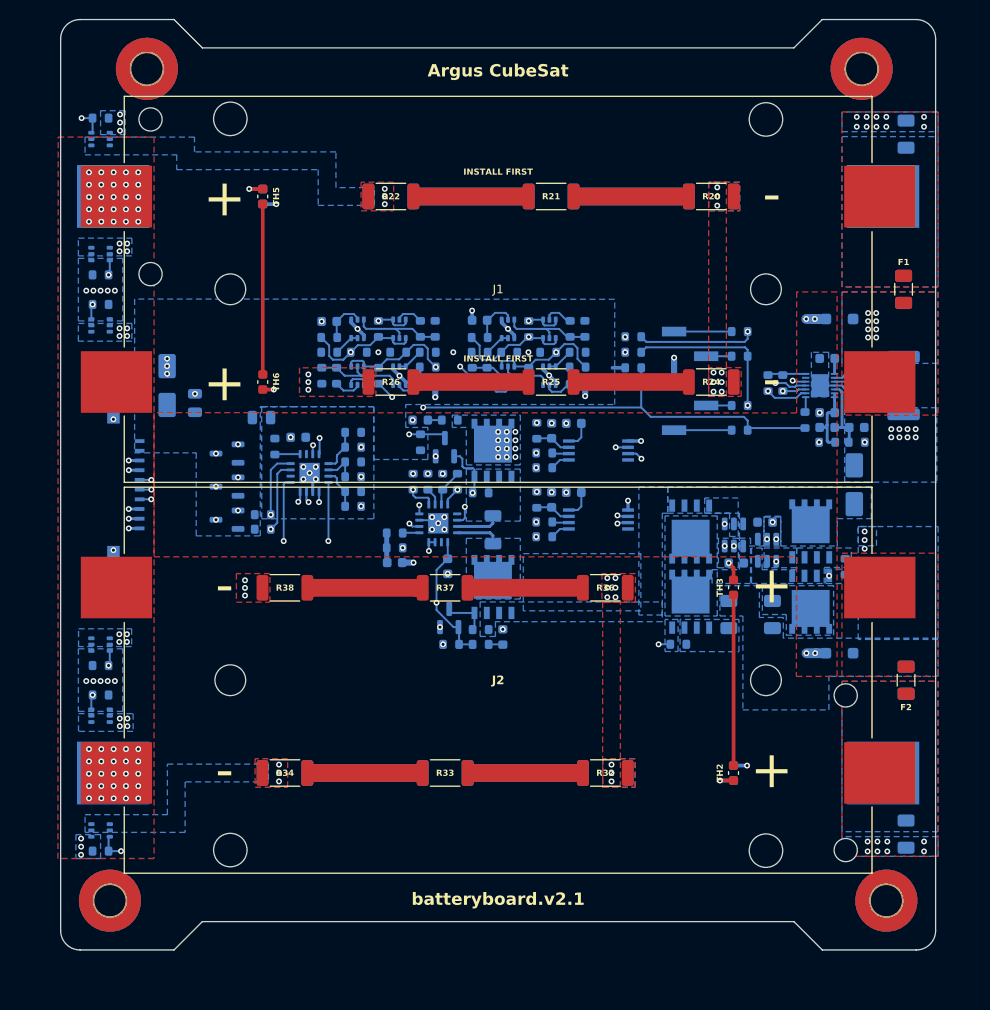
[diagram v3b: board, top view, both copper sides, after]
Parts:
- removed the REF** at (209.5, 59.2)
- added REF**: Val**, mainboard:XYZ_cubesat-top, B.Cu at (149.8, 109.7)
- Q3, Q5, Q6, Q7, R23, R31, R35, R43: moved to B.Cu
- moved D9 4.83 mm to (112.4, 100.4)
- moved D7 4.83 mm to (112.4, 97.0)
- moved D8 4.83 mm to (112.4, 93.6)
- moved F9 3.55 mm to (116.0, 89.9)
- moved D6 2.22 mm to (106.2, 86.6)
- moved C19 2.16 mm to (109.1, 88.4)
- moved R58 0.84 mm to (154.3, 84.8)
- moved R59 0.84 mm to (154.3, 81.6)
- moved R60 0.84 mm to (154.3, 83.2)
- moved R61 0.30 mm to (149.3, 80.8)
- moved R63 0.30 mm to (147.8, 80.8)
- moved Q17 0.20 mm to (145.6, 85.6)
- moved Q16 0.20 mm to (145.6, 80.8)
- moved R67 0.20 mm to (145.5, 83.2)
- moved C15 0.19 mm to (148.5, 86.5)
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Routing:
- net GND: track 17.1 -> 22.6 mm
- net /Interfaces/ALERT: track 82.0 -> 85.3 mm, vias 2 -> 3
- net /Interfaces/SDA_BUS: track 69.8 -> 71.8 mm, vias 3 -> 4
- net SYSTEM_VSS: track 26.4 -> 24.7 mm, vias 33 -> 32
- net /Battery Temperature Protection/HEATER_ENABLE1: track 73.6 -> 71.9 mm
- net +3V3: track 15.4 -> 16.8 mm
- net Net-(U6-AIN1): track 85.5 -> 86.6 mm
- net Net-(R25-Pad1): track 11.9 -> 10.8 mm
- net Net-(R37-Pad1): track 11.9 -> 10.9 mm
- net Net-(R28-Pad1): track 11.9 -> 11.0 mm
- net Net-(R41-Pad1): track 11.9 -> 11.0 mm
- net Net-(R29-Pad1): track 11.9 -> 11.0 mm
- net /Battery Monitor/I2C Protection/SDA_DEVICE: track 18.6 -> 19.4 mm
- net /Battery Monitor/SDA: track 26.1 -> 25.3 mm, vias 3 -> 2
- net /Battery Monitor/SCL: track 26.9 -> 26.0 mm
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- added copper zone on B.Cu, net Net-(Q3-D-Pad1)
- added copper zone on B.Cu, net Net-(Q5-D-Pad1)
- added copper zone on B.Cu, net Net-(Q6-D-Pad1)
- added copper zone on B.Cu, net Net-(Q7-D-Pad1)
- removed copper zone on B.Cu, net GND
- removed copper zone on F.Cu, net SYSTEM_VSS
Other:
- board text added: "ARGUS CubeSat Carnegie Mellon University BatteryBoard v2.1"
- board text added: "Argus CubeSat"
- board text added: "INSTALL FIRST"
- board text added: "Remove before flash"
- board text added: "TO MAINBOARD"
- board text added: "batteryboard.v2.1"
- board text removed: "ARGUS-2 CMU Cubesat BatteryBoard v1"
- board text removed: "MAINBOARD"
